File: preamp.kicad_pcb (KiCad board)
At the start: 2 copper layers, 95 x 44.9 mm, 95 parts, among them P1 GRCA1, P10 Jack_L, P11 Jack_R, P12 RCA2_L, P13 GND, P14 GND, P16 +15, P17 GND, P18 L_pow+, P19 R_pow+, P2 Inst_R, P20 L_pentode, P21 R_p, P22 L_pentode_in, P23 R_pentode_in, P27 R_pow-, P28 L_pow-, P29 GRM, P3 GND_instrum, P30 GRL, P31 GRH, P32 Gain_L_M, P33 Gain_L_L, P34 Gain_L_H, P35 LED_Ca, P36 SW_1, P37 SW_com, P38 SW_2, P39 LED_An, P4 RCA1_R, P40 vol_R_H, P41 vol_L_L, P42 vol_L_H, P43 vol_R_M, P44 vol_R_L, P45 vol_L_M, P5 Inst_L, P6 GRCA2, P7 RCA2_R, P8 RCA1_L, P9 GJack1, U1 LM193, U2 TL074, U3 TL074, U5 TLE2426, U6 LM7812, U7 DG419, U8 DG419

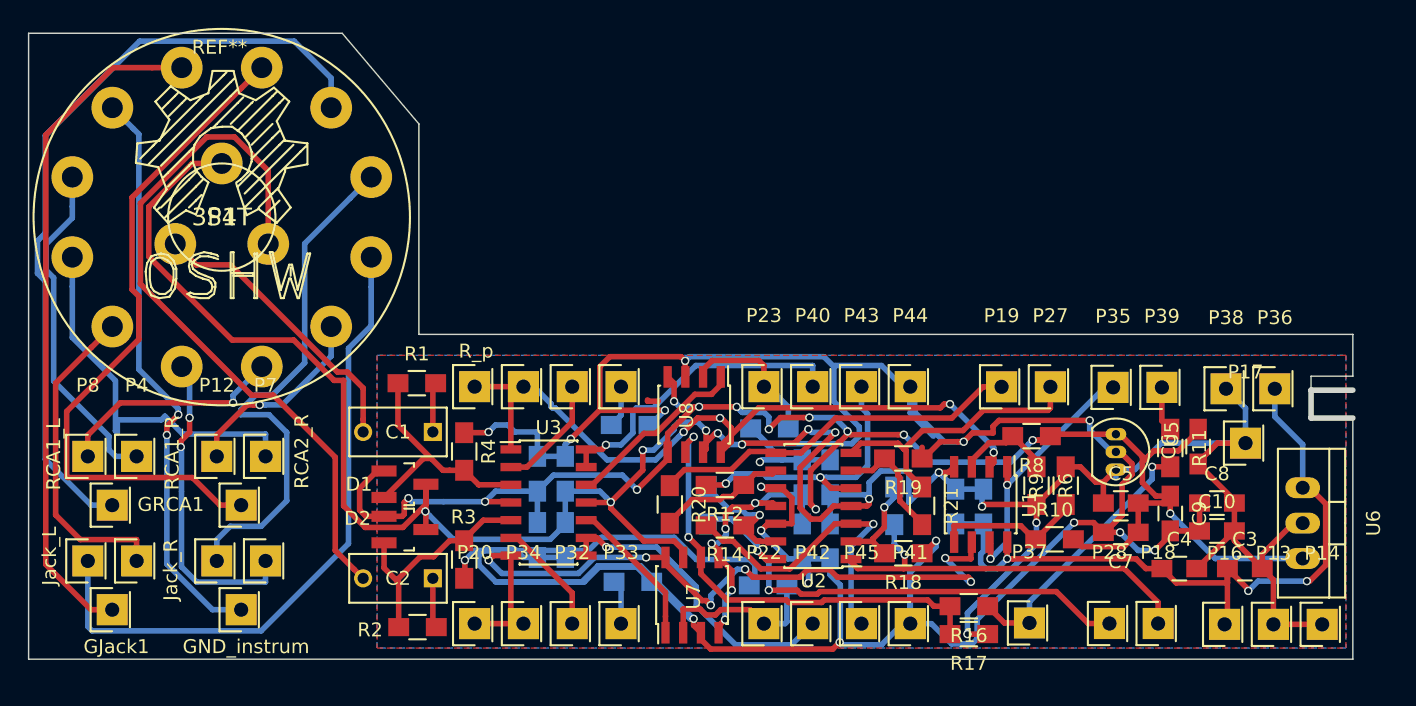
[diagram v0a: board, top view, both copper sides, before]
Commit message: Silkscreen fix
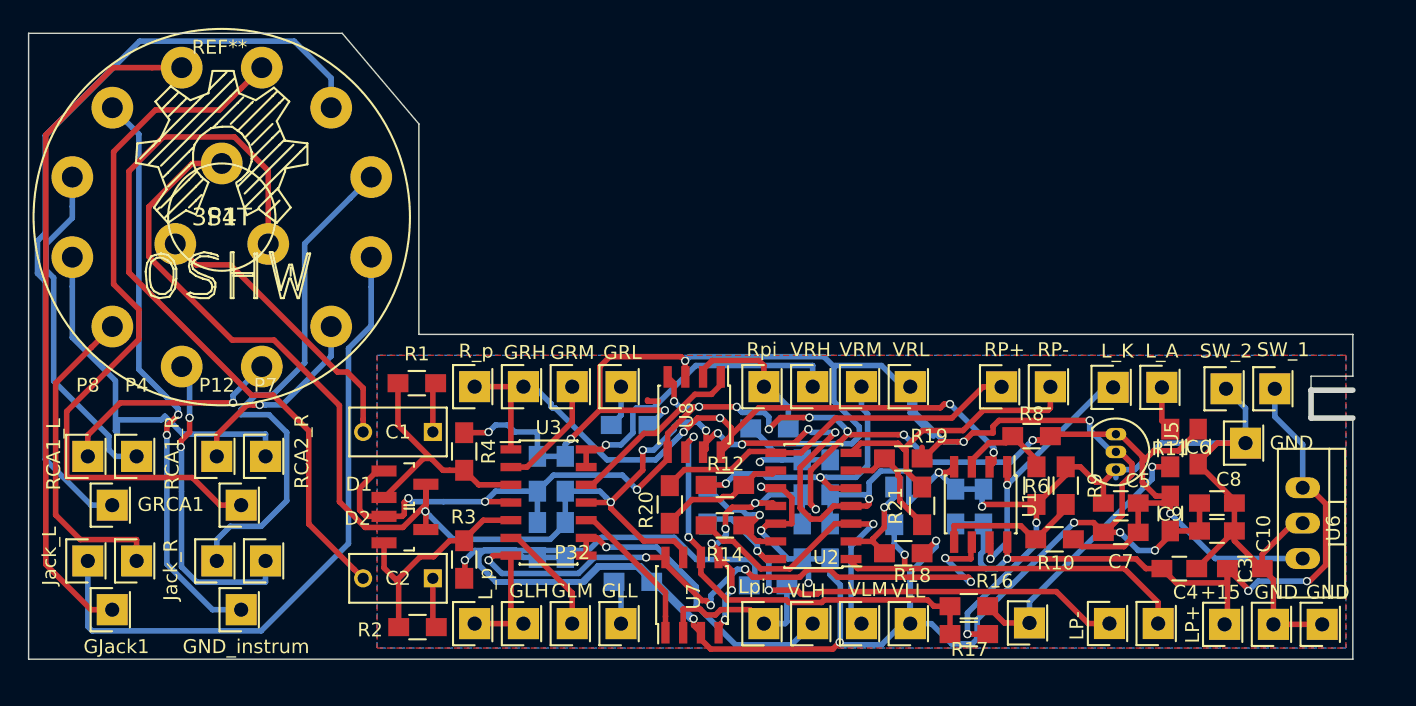
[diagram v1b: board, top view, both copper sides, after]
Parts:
- P18: value L_pow+ -> LP+
- P19: value R_pow+ -> RP+
- P20: value L_pentode -> L_p
- P22: value L_pentode_in -> Lpi
- P23: value R_pentode_in -> Rpi
- P27: value R_pow- -> RP-
- P28: value L_pow- -> LP-
- P32: value Gain_L_M -> GLM
- P33: value Gain_L_L -> GLL
- P34: value Gain_L_H -> GLH
- P35: value LED_Ca -> L_K
- P37: value SW_com -> SWC
- P39: value LED_An -> L_A
- P40: value vol_R_H -> VRH
- P41: value vol_L_L -> VLL
- P42: value vol_L_H -> VLH
- P43: value vol_R_M -> VRM
- P44: value vol_R_L -> VRL
- P45: value vol_L_M -> VLM
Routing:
- net Net-(P6-Pad1): track 48.9 -> 52.7 mm
- net Net-(C2-Pad2): track 51.8 -> 54.3 mm
- net -6VA: track 203.3 -> 202.1 mm

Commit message: 1M to gnd on all inputs
Added 1M to ground to avoid floating inputs
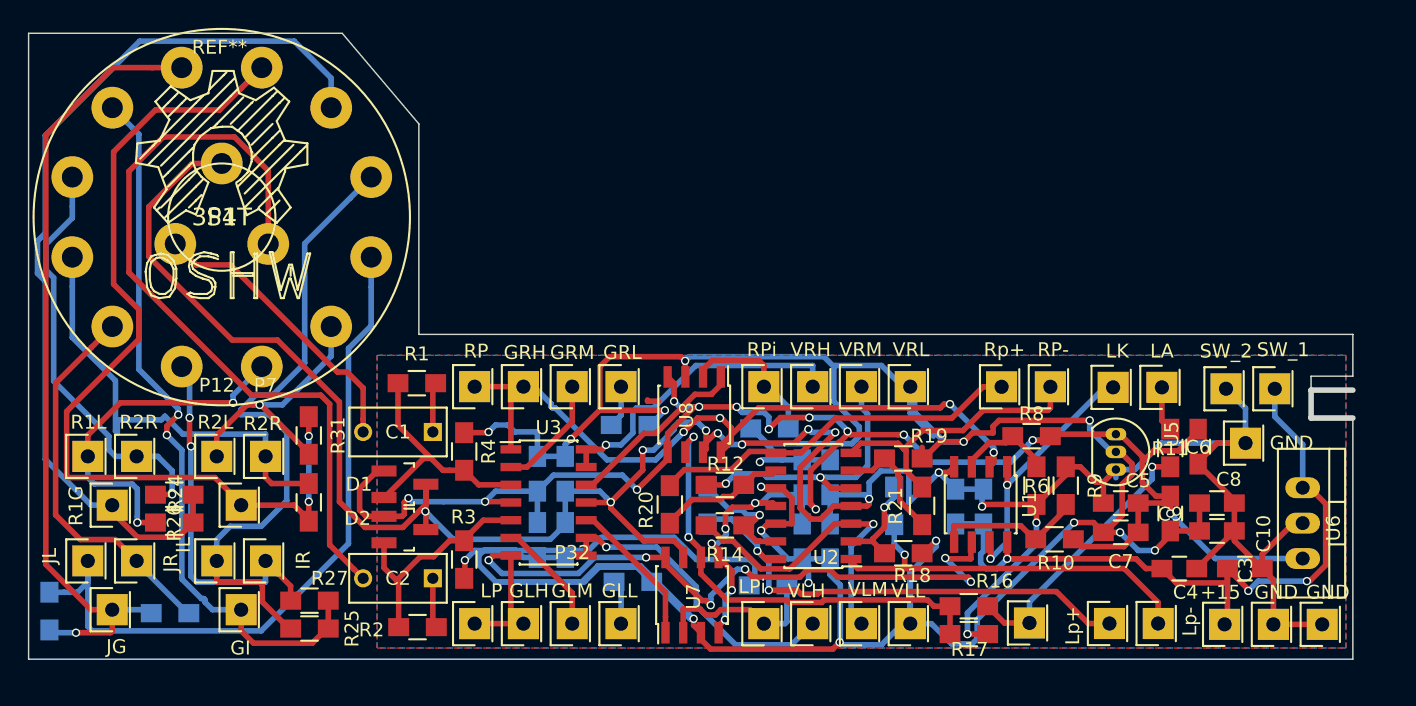
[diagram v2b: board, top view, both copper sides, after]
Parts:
- added R24: 1M, Resistors_SMD:R_0805_HandSoldering, F.Cu at (100.5, 73.5)
- added R25: 1M, Resistors_SMD:R_0805_HandSoldering, F.Cu at (110.2, 83.1)
- added R26: 1M, Resistors_SMD:R_0805_HandSoldering, F.Cu at (100.5, 75.5)
- added R27: 1M, Resistors_SMD:R_0805_HandSoldering, F.Cu at (110.2, 81.1)
- added R28: 1M, Resistors_SMD:R_0805_HandSoldering, B.Cu at (100.2, 82.0)
- added R29: 1M, Resistors_SMD:R_0805_HandSoldering, B.Cu at (91.5, 81.8)
- added R30: 1M, Resistors_SMD:R_0805_HandSoldering, F.Cu at (110.1, 74.0)
- added R31: 1M, Resistors_SMD:R_0805_HandSoldering, F.Cu at (110.1, 69.2)
- P1: value GRCA1 -> R1G
- P10: value Jack_L -> JL
- P11: value Jack_R -> JR
- P12: value RCA2_L -> R2L
- P18: value LP+ -> Lp-
- P19: value RP+ -> Rp+
- P2: value Inst_R -> IR
- P20: value L_p -> LP
- P21: value R_p -> RP
- P22: value Lpi -> LPi
- P23: value Rpi -> RPi
- P28: value LP- -> Lp+
- P3: value GND_instrum -> GI
- P35: value L_K -> LK
- P37: value SWC -> SW_com
- P39: value L_A -> LA
- P4: value RCA1_R -> R2R
- P5: value Inst_L -> IL
- P6: value GRCA2 -> R2G
- P7: value RCA2_R -> R2R
- P8: value RCA1_L -> R1L
- P9: value GJack1 -> JG
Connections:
- net -6VA renamed GND
- net Net-(P1-Pad1) renamed /GRCA
- net Net-(P3-Pad1) renamed /GI
- net Net-(P6-Pad1) renamed /GRCA2
- net Net-(P9-Pad1) renamed /GJ
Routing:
- net /GRCA2: track 52.7 -> 65.6 mm, vias 0 -> 2
- net /GI: track 41.7 -> 52.4 mm
- net /GRCA: track 56.4 -> 65.9 mm
- net Net-(P8-Pad1): track 16.4 -> 25.5 mm, vias 1 -> 2
- net /GJ: track 48.7 -> 57.7 mm, vias 0 -> 1
- net Net-(P5-Pad1): track 38.1 -> 47.0 mm
- net Net-(P4-Pad1): track 24.4 -> 30.3 mm, vias 0 -> 1
- net Net-(P12-Pad1): track 14.2 -> 19.2 mm
- net Net-(P7-Pad1): track 28.3 -> 33.1 mm
- net Net-(P10-Pad1): track 47.3 -> 51.9 mm
- net Net-(P11-Pad1): track 23.3 -> 27.7 mm
- net Net-(P2-Pad1): track 22.9 -> 26.0 mm
- net Net-(C2-Pad2): track 54.3 -> 56.3 mm
